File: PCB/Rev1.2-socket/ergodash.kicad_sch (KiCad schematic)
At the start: 87 parts, among them J1 5PIN, M1 Speaker, SW1 SW_PUSH, SW10 SW_PUSH, SW11 SW_PUSH, SW12 SW_PUSH, SW13 SW_PUSH, SW14 SW_PUSH, SW15 SW_PUSH, SW16 SW_PUSH, SW17 SW_PUSH, SW18 SW_PUSH, SW19 SW_PUSH, SW2 SW_PUSH, SW20 SW_PUSH, SW21 SW_PUSH, SW22 SW_PUSH, SW23 SW_PUSH, SW24 SW_PUSH, SW25 SW_PUSH, SW26 SW_PUSH, SW27 SW_PUSH, SW28 SW_PUSH, SW29 SW_Push, SW3 SW_PUSH, SW30 SW_PUSH, SW31 SW_PUSH, SW32 SW_PUSH, SW33 SW_PUSH, SW34 SW_PUSH, SW35 SW_PUSH, SW37 SW_Push, SW4 SW_PUSH, SW40 SW_PUSH, SW5 SW_PUSH, SW6 SW_PUSH, SW7 SW_PUSH, SW8 SW_PUSH, SW9 SW_PUSH, U1 HOLE, U2 HOLE, U3 ProMicro, U4 HOLE, U5 HOLE, U6 ProMicro, U7 HOLE, U8 HOLE, U9 HOLE

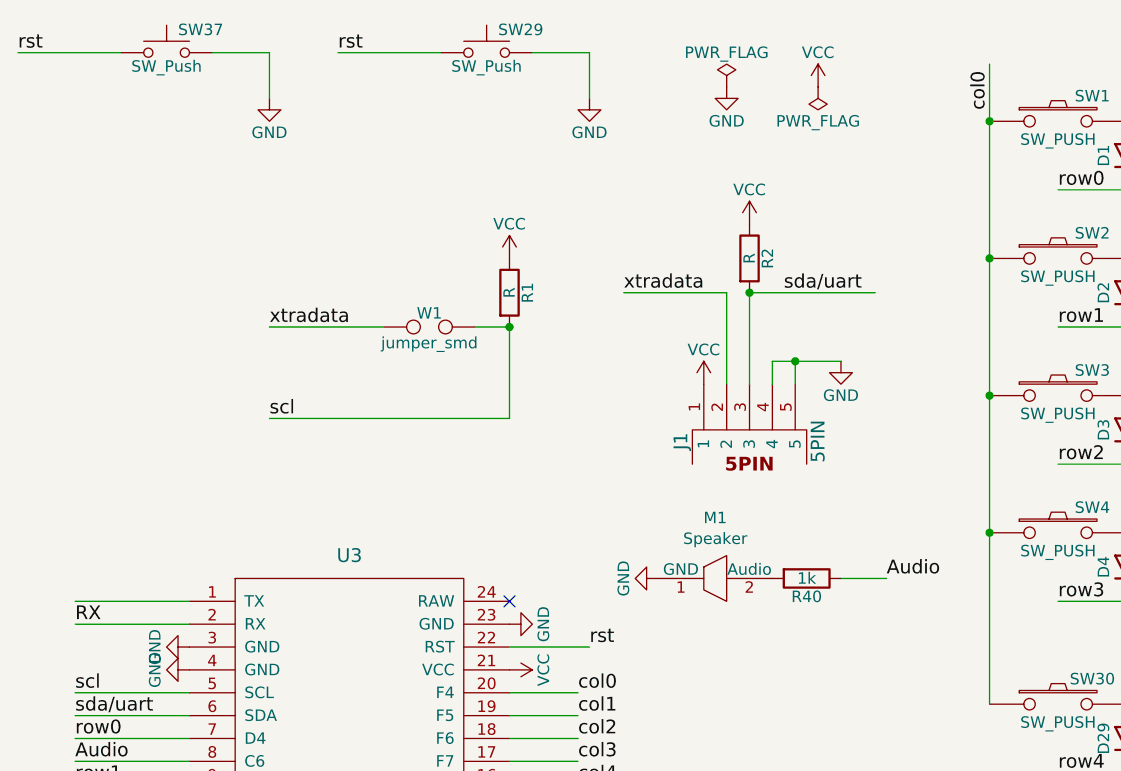
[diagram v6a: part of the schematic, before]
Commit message: Remove I2C/speaker options, add mascot logo, regenerate gerbers
- Remove the unpopulated I2C provision (pull-ups R1/R2, jumper W1) from
  schematic and board with its dead copper; split communication is QMK
  serial only (split.serial pin D0 = /sda/uart)
- Remove speaker M1 and its 1k resistor R40 (undocumented option absent
  from the build guide and shop list)
- Delete orphaned silk labels of removed options (V/G/RGB/I2C/Xtra/TX0/
  BL1k/Au1k); only the two nameplates remain, now reading
  "ErgoDash Rev. 1.2 / Socketed by tsubu" (also fixes the "Soket" typo)
- Restore bottom-row socket references SW30-SW35 that had drifted one
  step from the schematic (duplicate SW29, missing SW35)
- Add mascot logo footprint on both silkscreen sides and GND/VCC zones
- Regenerate manufacturing data into ergodash/ (verified in GerbView);
  drop the stale Rev1.2 gerber copies, originals live in PCB/Rev1.2/

Co-Authored-By: Claude Fable 5 <noreply@anthropic.com>
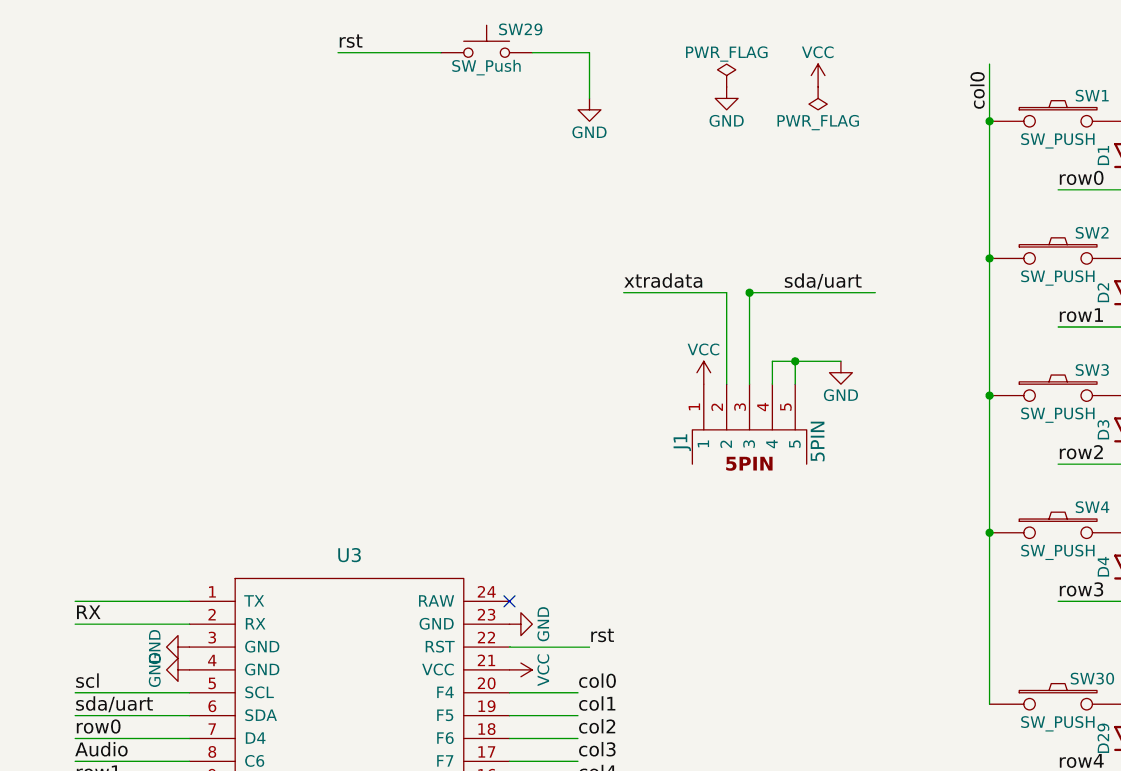
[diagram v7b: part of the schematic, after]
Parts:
- removed M1: Speaker, library:PKLCS1212E4001-R1, symbol ergodash:Speaker
- removed R1, R2: R, Resistors_THT:R_Axial_DIN0207_L6.3mm_D2.5mm_P10.16mm_Horizontal, symbol Device:R
- removed R40: 1k, Resistors_THT:R_Axial_DIN0207_L6.3mm_D2.5mm_P10.16mm_Horizontal, symbol Device:R
- removed SW37: SW_Push, library:tact_switch2, symbol switches:SW_Push
- removed W1: jumper_smd, library:jumper_smd_2dub, symbol ergodash:jumper_smd
